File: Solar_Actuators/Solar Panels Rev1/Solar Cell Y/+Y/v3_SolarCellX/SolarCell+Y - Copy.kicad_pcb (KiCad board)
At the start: 6 copper layers, 50 x 50 mm, 57 parts, among them IC1 symbols_TSL2561, J1 XF2M-1015-1A, J2 U.FL-R-SMT-1, U1 HHM17139B2, U2 Value

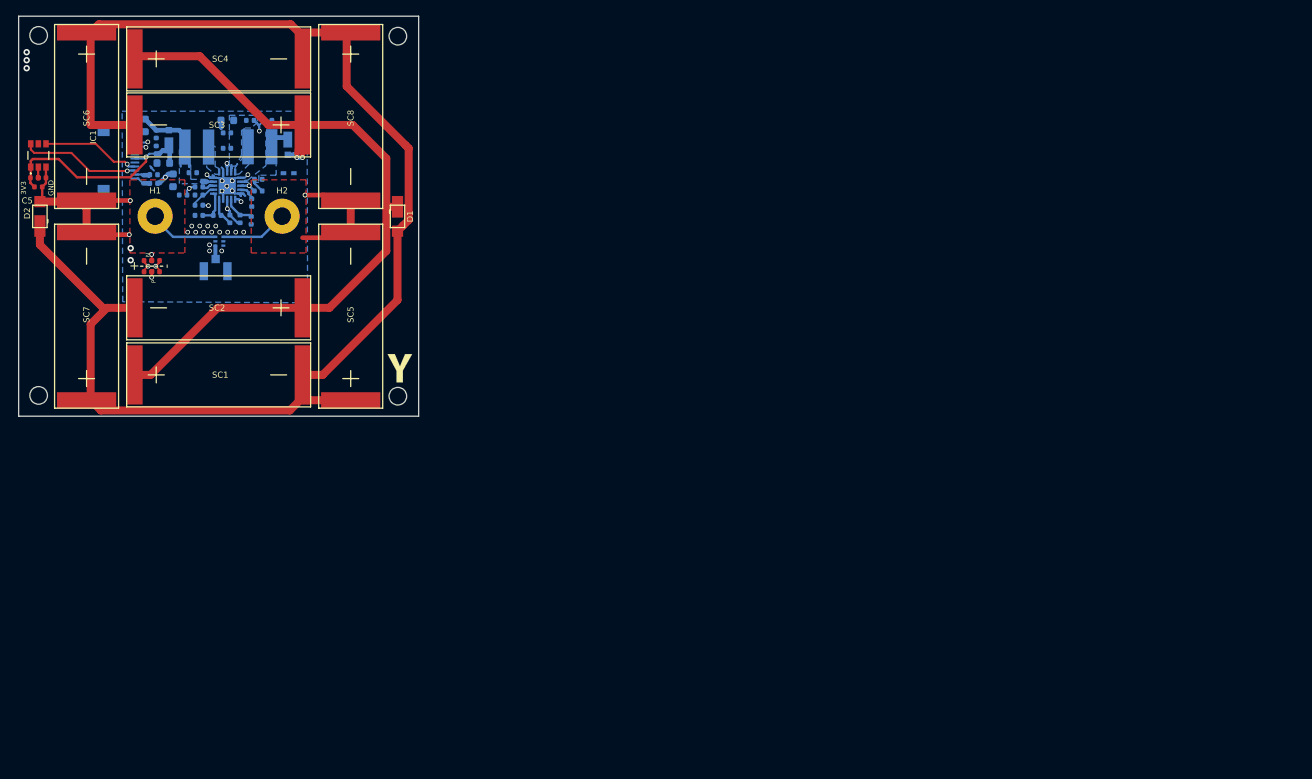
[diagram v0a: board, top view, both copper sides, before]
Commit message: +Y panel read for fab
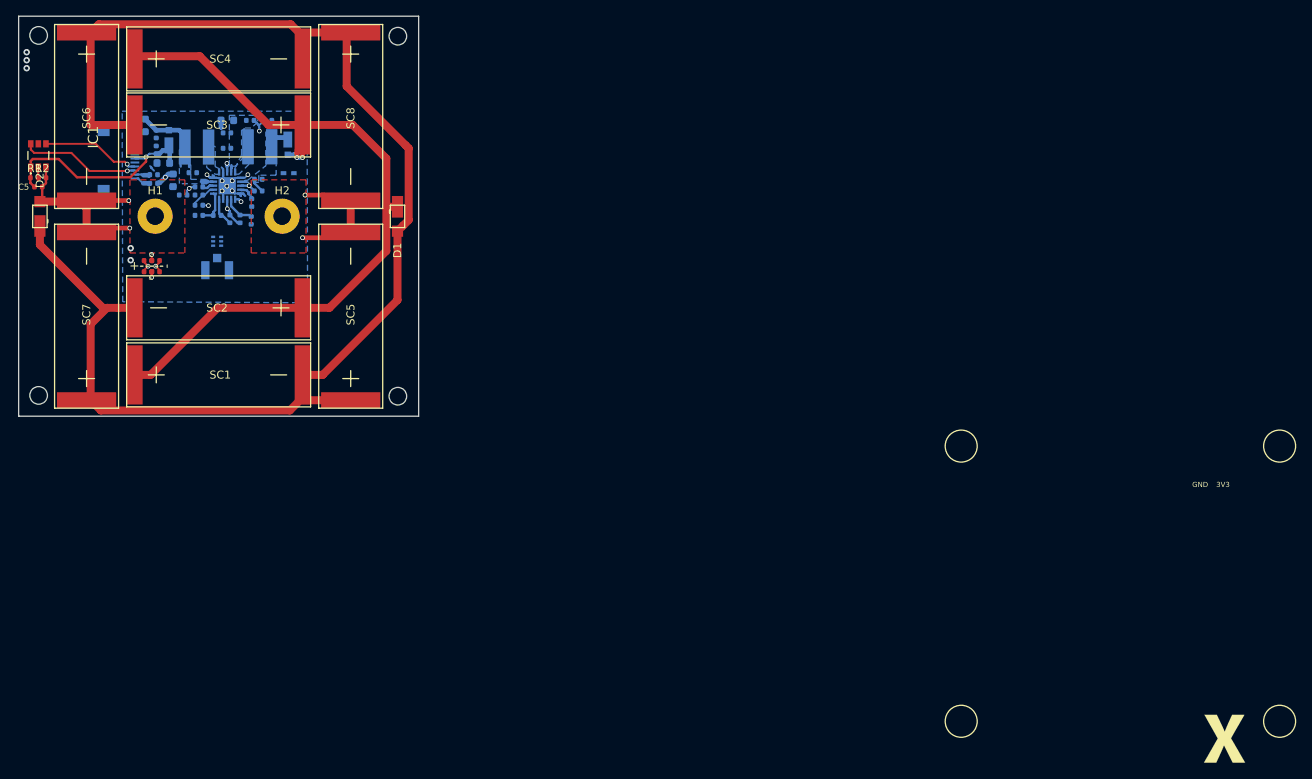
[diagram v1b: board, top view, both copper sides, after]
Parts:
- removed the Ref** at (215.6, 84.3)
- added Ref**: Val**, custom-footprints:xpanel, F.Cu at (317.6, 129.3)
- moved U1 0.27 mm to (174.8, 68.1)
- moved J2 0.23 mm to (174.8, 71.8)
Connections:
- U1 pad 3: Net-(H1-Pad1) -> Net-(H2-Pad1)
- U1 pad 4: Net-(H2-Pad1) -> Net-(H1-Pad1)
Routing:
- net /coil: track 14235.3 -> 3.61 mm, vias 7 -> 2
- net COIL_P: track 23.8 -> 14225.5 mm, vias 2 -> 6
- net COIL_N: track 18.5 -> 0.77 mm, vias 2 -> 1
- net Net-(H1-Pad1): track 10.2 -> 1.41 mm
- net Net-(H2-Pad1): track 8.42 -> 0.00 mm
- net Net-(J2-Pad3): track 1.43 -> 0.00 mm
- net GND: track 55.7 -> 55.6 mm, vias 25 -> 11
- removed copper zone on In3.Cu, net GND
